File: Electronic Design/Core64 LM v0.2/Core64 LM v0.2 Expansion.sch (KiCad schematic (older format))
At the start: 13 parts, among them J3 Conn_01x01_Male, J4 Conn_01x01_Male, J5 Conn_01x01_Male, J6 Conn_01x01_Male

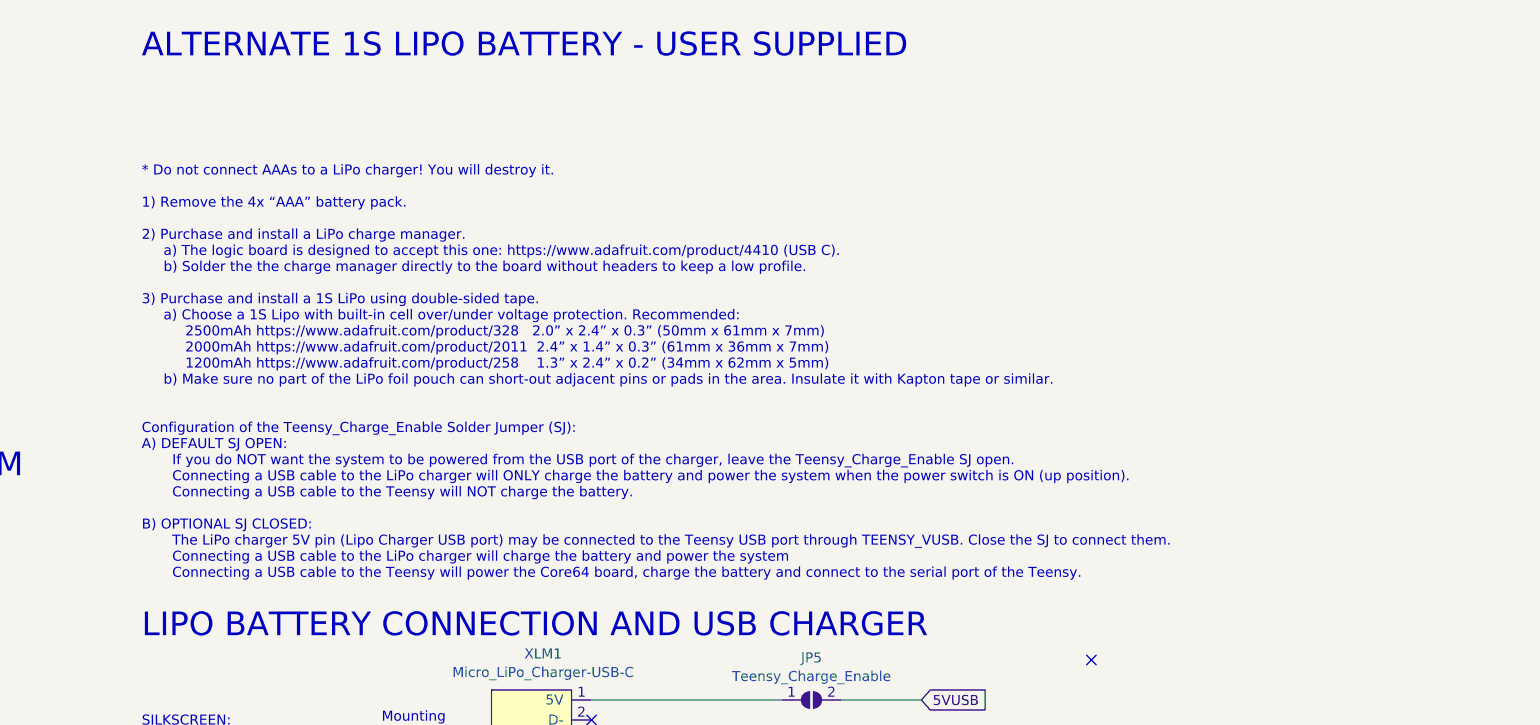
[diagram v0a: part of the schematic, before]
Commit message: Refine layout placement of QWIIC and silkscreen, add battery markers
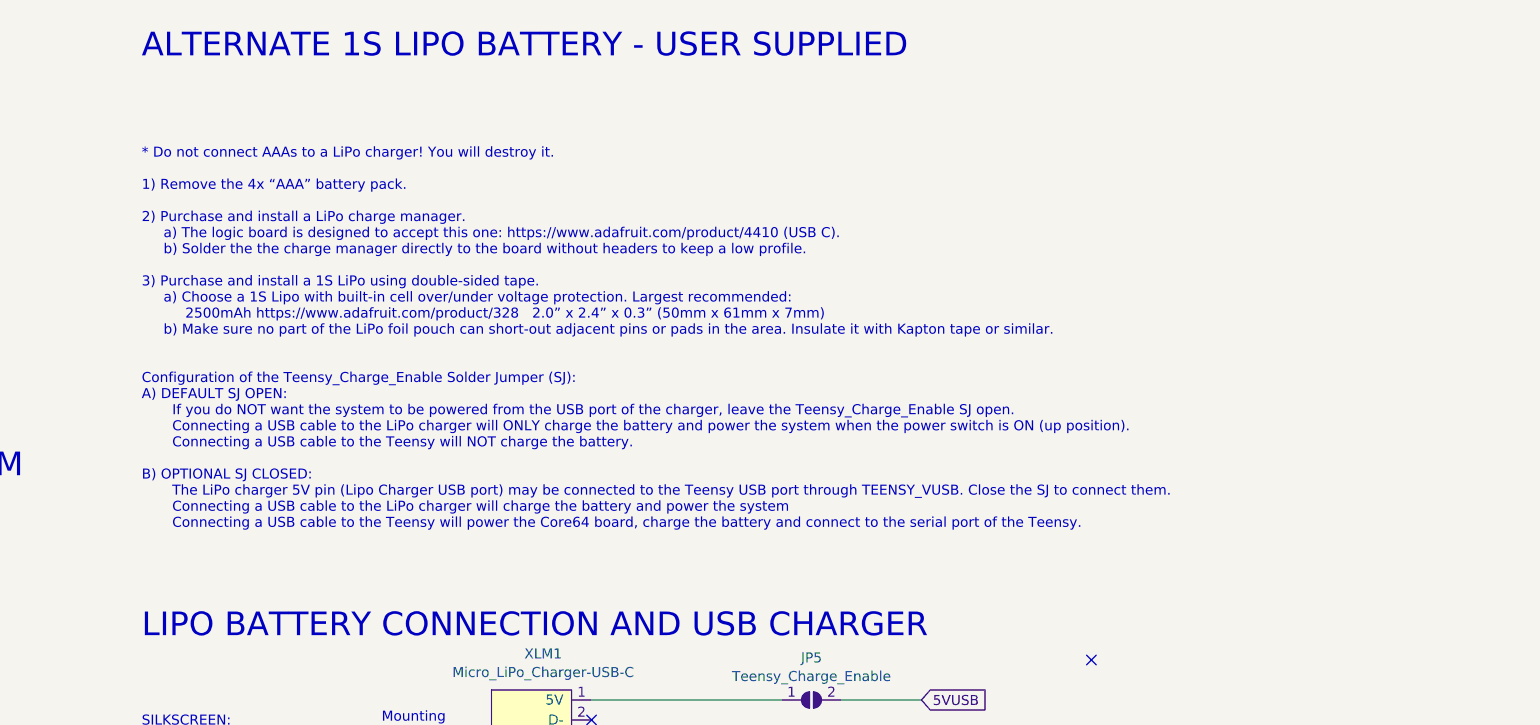
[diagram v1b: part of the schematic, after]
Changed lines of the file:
@@
 Text Notes 5500 4700 0    50   ~ 0
 Mounting\n5x 0.1” holes
-Text Notes 4300 3900 0    50   ~ 0
-* Do not connect AAAs to a LiPo charger! You will destroy it.\n\n1) Remove the 4x “AAA” battery pack.\n\n2) Purchase and install a LiPo charge manager.\n     a) The logic board is designed to accept this one: https://www.adafruit.com/product/4410 (USB C).\n     b) Solder the the charge manager directly to the board without headers to keep a low profile.\n\n3) Purchase and install a 1S LiPo using double-sided tape. \n     a) Choose a 1S Lipo with built-in cell over/under voltage protection. Recommended:\n          2500mAh https://www.adafruit.com/product/328   2.0” x 2.4” x 0.3” (50mm x 61mm x 7mm)\n          2000mAh https://www.adafruit.com/product/2011  2.4” x 1.4” x 0.3” (61mm x 36mm x 7mm)\n          1200mAh https://www.adafruit.com/product/258    1.3” x 2.4” x 0.2” (34mm x 62mm x 5mm)\n     b) Make sure no part of the LiPo foil pouch can short-out adjacent pins or pads in the area. Insulate it with Kapton tape or similar.\n\n\nConfiguration of the Teensy_Charge_Enable Solder Jumper (SJ):\nA) DEFAULT SJ OPEN:\n       If you do NOT want the system to be powered from the USB port of the charger, leave the Teensy_Charge_Enable SJ open.\n       Connecting a USB cable to the LiPo charger will ONLY charge the battery and power the system when the power switch is ON (up position).\n       Connecting a USB cable to the Teensy will NOT charge the battery.\n\nB) OPTIONAL SJ CLOSED:\n       The LiPo charger 5V pin (Lipo Charger USB port) may be connected to the Teensy USB port through TEENSY_VUSB. Close the SJ to connect them.\n       Connecting a USB cable to the LiPo charger will charge the battery and power the system \n       Connecting a USB cable to the Teensy will power the Core64 board, charge the battery and connect to the serial port of the Teensy.\n
+Text Notes 4300 3650 0    50   ~ 0
+* Do not connect AAAs to a LiPo charger! You will destroy it.\n\n1) Remove the 4x “AAA” battery pack.\n\n2) Purchase and install a LiPo charge manager.\n     a) The logic board is designed to accept this one: https://www.adafruit.com/product/4410 (USB C).\n     b) Solder the the charge manager directly to the board without headers to keep a low profile.\n\n3) Purchase and install a 1S LiPo using double-sided tape. \n     a) Choose a 1S Lipo with built-in cell over/under voltage protection. Largest recommended:\n          2500mAh https://www.adafruit.com/product/328   2.0” x 2.4” x 0.3” (50mm x 61mm x 7mm)\n     b) Make sure no part of the LiPo foil pouch can short-out adjacent pins or pads in the area. Insulate it with Kapton tape or similar.\n\n\nConfiguration of the Teensy_Charge_Enable Solder Jumper (SJ):\nA) DEFAULT SJ OPEN:\n       If you do NOT want the system to be powered from the USB port of the charger, leave the Teensy_Charge_Enable SJ open.\n       Connecting a USB cable to the LiPo charger will ONLY charge the battery and power the system when the power switch is ON (up position).\n       Connecting a USB cable to the Teensy will NOT charge the battery.\n\nB) OPTIONAL SJ CLOSED:\n       The LiPo charger 5V pin (Lipo Charger USB port) may be connected to the Teensy USB port through TEENSY_VUSB. Close the SJ to connect them.\n       Connecting a USB cable to the LiPo charger will charge the battery and power the system \n       Connecting a USB cable to the Teensy will power the Core64 board, charge the battery and connect to the serial port of the Teensy.\n
 Text Notes 800  3400 0    118  ~ 0
 OLED MONOCHROME I2C - BOTTOM

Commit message: Add "Teensy Charge Enable" to silkscreen
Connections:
- no-connect marks 3 -> 2
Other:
- note added: "SILKSCREEN:\nTEENSY CHARGE ENABLE"
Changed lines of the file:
@@
 NoConn ~ 6550 4600
 NoConn ~ 6550 4700
-NoConn ~ 9050 4300
 $Comp
 L Connector:Conn_01x01_Male J6
@@
 	1    0    0    -1
 $EndComp
+Text Notes 7700 4750 0    50   ~ 0
+SILKSCREEN:\nTEENSY CHARGE ENABLE
 $EndSCHEMATC

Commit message: Release LM V0.2 Gerbers and assembly files
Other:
- note added: "Diffuser layer alignment or mounting points"
- moved on the sheet: J3, J4, J5, J6
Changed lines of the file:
@@
 Sheet 2 2
 Title "Core64 LM (LED MATRIX)"
-Date "2021-03-08"
+Date "2021-03-21"
 Rev "0.2"
 Comp "Concept and design by Andy Geppert @ www.MachineIdeas.com"
 Comment1 "Visit www.Core64.io for information on assembly and optional features."
-Comment2 "*** As released 2021-03-xx ***"
+Comment2 "*** As released 2021-03-21 ***"
 Comment3 ""
 Comment4 "All capacitors ceramic X7R unless otherwise noted."
@@
 L Connector:Conn_01x01_Male J6
 U 1 1 60516F1B
-P 4200 7300
-F 0 "J6" H 4309 7487 50  0000 C CNN
-F 1 "Conn_01x01_Male" H 4309 7394 50  0000 C CNN
-F 2 "Connector_PinHeader_2.54mm:PinHeader_1x01_P2.54mm_Vertical_No_Registration" H 4200 7300 50  0001 C CNN
-F 3 "~" H 4200 7300 50  0001 C CNN
-	1    4200 7300
+P 4200 7550
+F 0 "J6" H 4309 7737 50  0000 C CNN
+F 1 "Conn_01x01_Male" H 4309 7644 50  0000 C CNN
+F 2 "Connector_PinHeader_2.54mm:PinHeader_1x01_P2.54mm_Vertical_No_Registration" H 4200 7550 50  0001 C CNN
+F 3 "~" H 4200 7550 50  0001 C CNN
+	1    4200 7550
 	1    0    0    -1
 $EndComp
@@
 L Connector:Conn_01x01_Male J4
 U 1 1 6051423B
-P 2500 7300
-F 0 "J4" H 2609 7487 50  0000 C CNN
-F 1 "Conn_01x01_Male" H 2609 7394 50  0000 C CNN
-F 2 "Connector_PinHeader_2.54mm:PinHeader_1x01_P2.54mm_Vertical_No_Registration" H 2500 7300 50  0001 C CNN
-F 3 "~" H 2500 7300 50  0001 C CNN
-	1    2500 7300
+P 2500 7550
+F 0 "J4" H 2609 7737 50  0000 C CNN
+F 1 "Conn_01x01_Male" H 2609 7644 50  0000 C CNN
+F 2 "Connector_PinHeader_2.54mm:PinHeader_1x01_P2.54mm_Vertical_No_Registration" H 2500 7550 50  0001 C CNN
+F 3 "~" H 2500 7550 50  0001 C CNN
+	1    2500 7550
 	1    0    0    -1
 $EndComp
@@
 L Connector:Conn_01x01_Male J3
 U 1 1 6051203C
-P 1650 7300
-F 0 "J3" H 1759 7487 50  0000 C CNN
-F 1 "Conn_01x01_Male" H 1759 7394 50  0000 C CNN
-F 2 "Connector_PinHeader_2.54mm:PinHeader_1x01_P2.54mm_Vertical_No_Registration" H 1650 7300 50  0001 C CNN
-F 3 "~" H 1650 7300 50  0001 C CNN
-	1    1650 7300
+P 1650 7550
+F 0 "J3" H 1759 7737 50  0000 C CNN
+F 1 "Conn_01x01_Male" H 1759 7644 50  0000 C CNN
+F 2 "Connector_PinHeader_2.54mm:PinHeader_1x01_P2.54mm_Vertical_No_Registration" H 1650 7550 50  0001 C CNN
+F 3 "~" H 1650 7550 50  0001 C CNN
+	1    1650 7550
 	1    0    0    -1
 $EndComp
@@
 L Connector:Conn_01x01_Male J5
 U 1 1 60515800
-P 3350 7300
-F 0 "J5" H 3459 7487 50  0000 C CNN
-F 1 "Conn_01x01_Male" H 3459 7394 50  0000 C CNN
-F 2 "Connector_PinHeader_2.54mm:PinHeader_1x01_P2.54mm_Vertical_No_Registration" H 3350 7300 50  0001 C CNN
-F 3 "~" H 3350 7300 50  0001 C CNN
-	1    3350 7300
+P 3350 7550
+F 0 "J5" H 3459 7737 50  0000 C CNN
+F 1 "Conn_01x01_Male" H 3459 7644 50  0000 C CNN
+F 2 "Connector_PinHeader_2.54mm:PinHeader_1x01_P2.54mm_Vertical_No_Registration" H 3350 7550 50  0001 C CNN
+F 3 "~" H 3350 7550 50  0001 C CNN
+	1    3350 7550
 	1    0    0    -1
 $EndComp
@@
 L power:GND #PWR?
 U 1 1 607ECE86
-P 1850 7300
+P 1850 7550
 AR Path="/607ECE86" Ref="#PWR?"  Part="1"
 AR Path="/603A0E05/607ECE86" Ref="#PWR0111"  Part="1"
-F 0 "#PWR0111" H 1850 7050 50  0001 C CNN
-F 1 "GND" H 1855 7123 50  0000 C CNN
-F 2 "" H 1850 7300 50  0001 C CNN
-F 3 "" H 1850 7300 50  0001 C CNN
-	1    1850 7300
+F 0 "#PWR0111" H 1850 7300 50  0001 C CNN
+F 1 "GND" H 1855 7373 50  0000 C CNN
+F 2 "" H 1850 7550 50  0001 C CNN
+F 3 "" H 1850 7550 50  0001 C CNN
+	1    1850 7550
 	1    0    0    -1
 $EndComp
@@
 L power:GND #PWR?
 U 1 1 607EDA9C
-P 2700 7300
+P 2700 7550
 AR Path="/607EDA9C" Ref="#PWR?"  Part="1"
 AR Path="/603A0E05/607EDA9C" Ref="#PWR0112"  Part="1"
-F 0 "#PWR0112" H 2700 7050 50  0001 C CNN
-F 1 "GND" H 2705 7123 50  0000 C CNN
-F 2 "" H 2700 7300 50  0001 C CNN
-F 3 "" H 2700 7300 50  0001 C CNN
-	1    2700 7300
+F 0 "#PWR0112" H 2700 7300 50  0001 C CNN
+F 1 "GND" H 2705 7373 50  0000 C CNN
+F 2 "" H 2700 7550 50  0001 C CNN
+F 3 "" H 2700 7550 50  0001 C CNN
+	1    2700 7550
 	1    0    0    -1
 $EndComp
@@
 L power:GND #PWR?
 U 1 1 607EE7C2
-P 3550 7300
+P 3550 7550
 AR Path="/607EE7C2" Ref="#PWR?"  Part="1"
 AR Path="/603A0E05/607EE7C2" Ref="#PWR0113"  Part="1"
-F 0 "#PWR0113" H 3550 7050 50  0001 C CNN
-F 1 "GND" H 3555 7123 50  0000 C CNN
-F 2 "" H 3550 7300 50  0001 C CNN
-F 3 "" H 3550 7300 50  0001 C CNN
-	1    3550 7300
+F 0 "#PWR0113" H 3550 7300 50  0001 C CNN
+F 1 "GND" H 3555 7373 50  0000 C CNN
+F 2 "" H 3550 7550 50  0001 C CNN
+F 3 "" H 3550 7550 50  0001 C CNN
+	1    3550 7550
 	1    0    0    -1
 $EndComp
@@
 L power:GND #PWR?
 U 1 1 607EF44F
-P 4400 7300
+P 4400 7550
 AR Path="/607EF44F" Ref="#PWR?"  Part="1"
 AR Path="/603A0E05/607EF44F" Ref="#PWR0114"  Part="1"
-F 0 "#PWR0114" H 4400 7050 50  0001 C CNN
-F 1 "GND" H 4405 7123 50  0000 C CNN
-F 2 "" H 4400 7300 50  0001 C CNN
-F 3 "" H 4400 7300 50  0001 C CNN
-	1    4400 7300
+F 0 "#PWR0114" H 4400 7300 50  0001 C CNN
+F 1 "GND" H 4405 7373 50  0000 C CNN
+F 2 "" H 4400 7550 50  0001 C CNN
+F 3 "" H 4400 7550 50  0001 C CNN
+	1    4400 7550
 	1    0    0    -1
 $EndComp
 Text Notes 7700 4750 0    50   ~ 0
 SILKSCREEN:\nTEENSY CHARGE ENABLE
+Text Notes 800  7200 0    118  ~ 0
+Diffuser layer alignment or mounting points
 $EndSCHEMATC
